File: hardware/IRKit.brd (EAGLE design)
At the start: 54 x 56 mm, 71 parts, among them CN1 ZX62-B-5PA(11), IC1 ATMEGA32U4AU, IC2 TLV70233DBVT, IC3 LM386MM-1, IC4 GS1011MXXS, SW1 EVQPUJ02K, T1 2SD1781KT146Q, T2 BSS138

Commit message: change R2,R8 value to 5.1k to reduce current
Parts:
- LED1: value 5V -> OSG50805C1C
- R2: value 910 -> 5.1k
- R8: value 1k -> 5.1k
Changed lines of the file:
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@@
 <dimension x1="22" y1="56" x2="22" y2="55" x3="21.4" y3="55.5" textsize="1.778" layer="51"/>
 <text x="47.9" y="15.1" size="0.8128" layer="21" rot="R90">+3.3V</text>
+<dimension x1="24.375" y1="5" x2="29.625" y2="5" x3="27" y3="-9" textsize="1.778" layer="51" dtype="horizontal"/>
 </plain>
 <attributes>
@@
 </autorouter>
 <elements>
-<element name="R2" library="my" package="SMD2012" value="910" x="27.85" y="50.975" smashed="yes" rot="R90">
+<element name="R2" library="my" package="SMD2012" value="5.1k" x="27.85" y="50.975" smashed="yes" rot="R90">
 <attribute name="NAME" x="27.193" y="52.901" size="0.8128" layer="25"/>
 <attribute name="VALUE" x="30.136" y="50.213" size="0.8128" layer="27" rot="R90"/>
@@
 <attribute name="VALUE" x="27.282" y="50.2115" size="0.8128" layer="27" rot="R90"/>
 </element>
-<element name="LED1" library="my" package="LED2012" value="5V" x="30.8625" y="51.925" smashed="yes">
+<element name="LED1" library="my" package="LED2012" value="OSG50805C1C" x="30.8625" y="51.925" smashed="yes">
 <attribute name="NAME" x="29.2405" y="52.941" size="0.8128" layer="25"/>
 <attribute name="VALUE" x="30.1005" y="49.639" size="0.8128" layer="27"/>
@@
 <attribute name="VALUE" x="17.086" y="14.438" size="0.8128" layer="27" rot="R90"/>
 </element>
-<element name="R8" library="my" package="SMD2012" value="1k" x="36.4" y="49.9" smashed="yes">
+<element name="R8" library="my" package="SMD2012" value="5.1k" x="36.4" y="49.9" smashed="yes">
 <attribute name="NAME" x="38.338" y="49.416" size="0.8128" layer="25"/>
 <attribute name="VALUE" x="35.638" y="47.614" size="0.8128" layer="27"/>

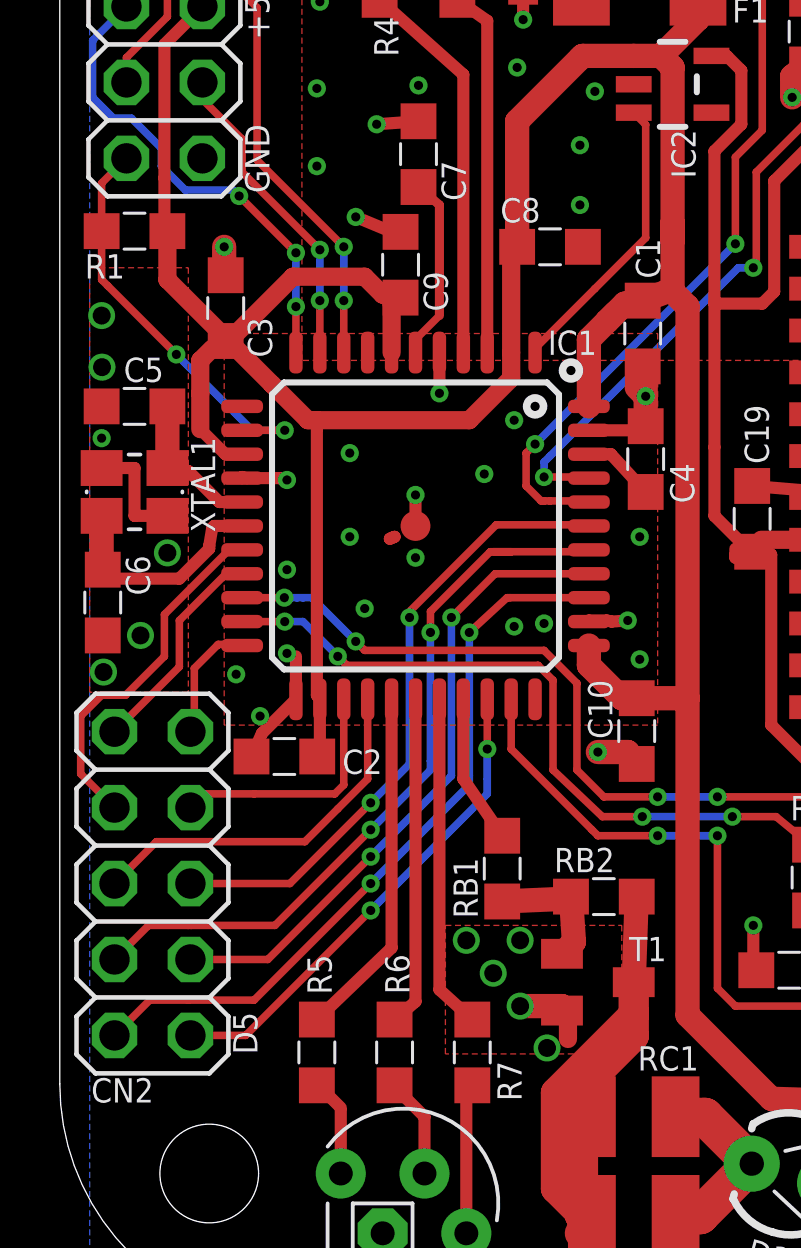
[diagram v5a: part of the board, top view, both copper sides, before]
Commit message: make lines around T1 thinner, because it took long to warm T1's emitter pad move R1 a little bit far from ICSP header, not to conflict with it
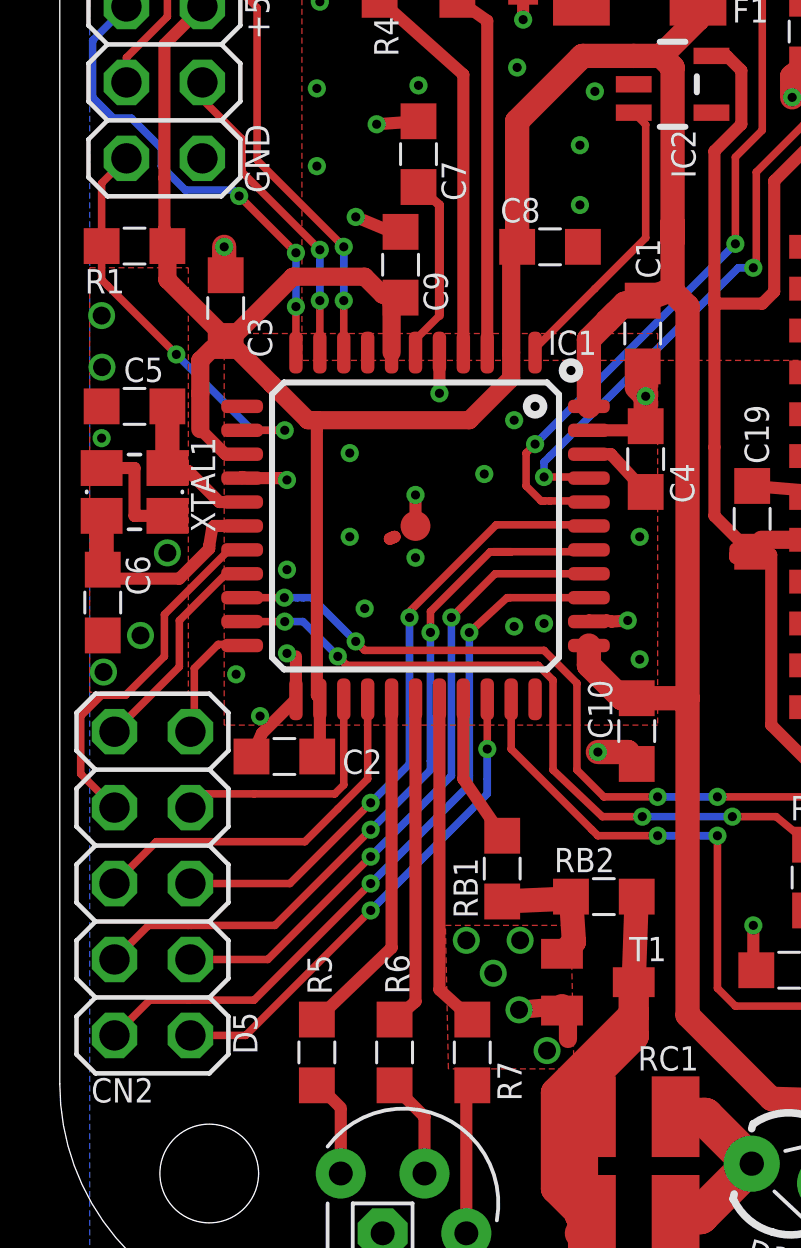
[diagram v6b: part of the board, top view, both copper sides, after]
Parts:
- moved R1 0.50 mm to (2.50, 36.0)
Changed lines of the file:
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@@
 <attribute name="VALUE" x="8.914" y="9.812" size="0.8128" layer="27" rot="R270"/>
 </element>
-<element name="R1" library="my" package="SMD2012" value="10k" x="2.5" y="36.525" smashed="yes">
-<attribute name="NAME" x="0.838" y="34.941" size="0.8128" layer="25"/>
-<attribute name="VALUE" x="0.638" y="35.739" size="0.8128" layer="27"/>
+<element name="R1" library="my" package="SMD2012" value="10k" x="2.5" y="36.025" smashed="yes">
+<attribute name="NAME" x="0.838" y="34.441" size="0.8128" layer="25"/>
+<attribute name="VALUE" x="0.638" y="35.239" size="0.8128" layer="27"/>
 </element>
 <element name="RB2" library="my" package="SMD2012" value="10k" x="18.2" y="14.2625" smashed="yes">
@@
 <wire x1="1.6" y1="34.7" x2="3.9" y2="32.4" width="0.254" layer="1"/>
 <wire x1="1.6" y1="34.7" x2="1.4" y2="34.9" width="0.254" layer="1"/>
-<wire x1="1.4" y1="34.9" x2="1.4" y2="36.525" width="0.254" layer="1"/>
-<wire x1="1.4" y1="36.525" x2="1.4" y2="38.13" width="0.254" layer="1"/>
+<wire x1="1.4" y1="34.9" x2="1.4" y2="36.025" width="0.254" layer="1"/>
+<wire x1="1.4" y1="36.025" x2="1.4" y2="38.13" width="0.254" layer="1"/>
 <wire x1="1.4" y1="38.13" x2="2.23" y2="38.96" width="0.254" layer="1"/>
 </signal>
@@
 <wire x1="17.7" y1="22" x2="17.7" y2="22.6625" width="0.8128" layer="1"/>
 <wire x1="5.55" y1="32.95" x2="3.6" y2="34.9" width="0.6096" layer="1"/>
-<wire x1="3.6" y1="34.9" x2="3.6" y2="36.525" width="0.6096" layer="1"/>
+<wire x1="3.6" y1="34.9" x2="3.6" y2="36.025" width="0.6096" layer="1"/>
 <wire x1="3.5" y1="38.3" x2="3.5" y2="36.625" width="0.4064" layer="1"/>
-<wire x1="3.5" y1="36.625" x2="3.6" y2="36.525" width="0.4064" layer="1"/>
+<wire x1="3.5" y1="36.625" x2="3.6" y2="36.025" width="0.4064" layer="1"/>
 <wire x1="19.3" y1="20.9" x2="18.8" y2="20.9" width="0.8128" layer="1"/>
 <wire x1="18.8" y1="20.9" x2="17.7" y2="22" width="0.8128" layer="1"/>
@@
 <via x="17.4" y="39.4" extent="1-16" drill="0.3048"/>
 <wire x1="19.6" y1="31" x2="19.6" y2="30" width="0.8128" layer="1"/>
-<polygon width="0.8128" layer="1">
+<polygon width="0.6096" layer="1">
 <vertex x="12.9" y="13.3"/>
-<vertex x="18.8" y="13.3"/>
-<vertex x="18.8" y="9"/>
-<vertex x="12.9" y="9"/>
+<vertex x="17.1" y="13.3"/>
+<vertex x="17.2" y="8.5"/>
+<vertex x="13" y="8.5"/>
 </polygon>
 <via x="13.6" y="53.0875" extent="1-16" drill="0.3048"/>
@@
 <wire x1="23.3" y1="11.8" x2="23.2" y2="12.1" width="0.4064" layer="1"/>
 <wire x1="23.2" y1="12.1" x2="23.2" y2="13.3" width="0.4064" layer="1"/>
-<via x="15.4" y="10.6" extent="1-16" drill="0.6"/>
+<via x="15.3625" y="10.475" extent="1-16" drill="0.6"/>
 <wire x1="31.8625" y1="51.925" x2="31.8875" y2="51.9" width="0.4064" layer="1"/>
 <wire x1="31.8875" y1="51.9" x2="33" y2="51.9" width="0.8128" layer="1"/>
@@
 <contactref element="T1" pad="E"/>
 <wire x1="16.8" y1="10.45" x2="17" y2="10.45" width="0.6096" layer="1"/>
-<wire x1="15.4" y1="10.6" x2="16.8" y2="10.6" width="0.8128" layer="1"/>
+<wire x1="15.3625" y1="10.475" x2="16.8" y2="10.6" width="0.6096" layer="1"/>
 <wire x1="16.8" y1="10.6" x2="16.8" y2="10.45" width="0.8128" layer="1"/>
 <wire x1="17" y1="10.45" x2="17" y2="9.5" width="0.6096" layer="1"/>
-<via x="16.3" y="9.2" extent="1-16" drill="0.6"/>
+<via x="16.3" y="9.1125" extent="1-16" drill="0.6"/>
 <via x="14.5" y="11.7" extent="1-16" drill="0.6"/>
 <via x="3.6" y="25.7625" extent="1-16" drill="0.6"/>

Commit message: added LED CAP
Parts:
- added LEDCAP1: LED-CAP, my:LED-CAP
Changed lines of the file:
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@@
 <attribute name="VALUE" x="0.9" y="25.55" size="1.27" layer="27"/>
 </element>
+<element name="LEDCAP1" library="my" package="LED-CAP" value="LED-CAP" x="10.8" y="-1.5"/>
 </elements>
 <signals>

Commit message: added screws updated microphone input resistor value 2k -> 2.2k change voltage dividing resistors values 2k/3.3k -> 3.3k/5.1k
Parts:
- added SCREW1, SCREW2, SCREW3, SCREW4: flat-head M3 self-tapping, my:SCREW-M3
- MIC: value kus0223 -> kus0323
- R14: value 1.3k -> 3.3k
- R15: value 2k -> 2.2k
- R16: value 2k -> 5.1k
- moved LEDCAP1 1.06 mm to (11.5, -0.70)
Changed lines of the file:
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@@
 <attribute name="VALUE" x="33.14" y="50.802" size="1.27" layer="27" ratio="10" rot="R180"/>
 </element>
-<element name="MIC" library="my" package="MIC_SMD_4MM" value="kus0223" x="42.8" y="49" smashed="yes">
+<element name="MIC" library="my" package="MIC_SMD_4MM" value="kus0323" x="42.8" y="49" smashed="yes">
 <attribute name="NAME" x="44.7" y="50.5" size="0.8128" layer="25"/>
 <attribute name="VALUE" x="44.7" y="46.8" size="0.8128" layer="27"/>
 </element>
-<element name="R15" library="my" package="SMD2012" value="2k" x="44.8" y="45.5" smashed="yes">
+<element name="R15" library="my" package="SMD2012" value="2.2k" x="44.8" y="45.5" smashed="yes">
 <attribute name="NAME" x="46.7" y="44.975" size="0.8128" layer="25"/>
 <attribute name="VALUE" x="43.8" y="43.6" size="1.016" layer="27"/>
 </element>
-<element name="R14" library="my" package="SMD2012" value="1.3k" x="44.8" y="43" smashed="yes" rot="R180">
+<element name="R14" library="my" package="SMD2012" value="3.3k" x="44.8" y="43" smashed="yes" rot="R180">
 <attribute name="NAME" x="46.7" y="42.575" size="0.8128" layer="25"/>
 <attribute name="VALUE" x="45.8" y="44.9" size="1.016" layer="27" rot="R180"/>
 </element>
-<element name="R16" library="my" package="SMD2012" value="2k" x="44.8" y="40.4" smashed="yes">
+<element name="R16" library="my" package="SMD2012" value="5.1k" x="44.8" y="40.4" smashed="yes">
 <attribute name="NAME" x="46.6875" y="39.9125" size="0.8128" layer="25"/>
 <attribute name="VALUE" x="43.8" y="38.5" size="1.016" layer="27"/>
@@
 <attribute name="VALUE" x="0.9" y="25.55" size="1.27" layer="27"/>
 </element>
-<element name="LEDCAP1" library="my" package="LED-CAP" value="LED-CAP" x="10.8" y="-1.5"/>
+<element name="LEDCAP1" library="my" package="LED-CAP" value="LED-CAP" x="11.5" y="-0.7"/>
+<element name="SCREW1" library="my" package="SCREW-M3" value="flat-head M3 self-tapping" x="-7.4" y="-11.1"/>
+<element name="SCREW2" library="my" package="SCREW-M3" value="flat-head M3 self-tapping" x="-8.4" y="-12.2"/>
+<element name="SCREW3" library="my" package="SCREW-M3" value="flat-head M3 self-tapping" x="-9.4" y="-13.3"/>
+<element name="SCREW4" library="my" package="SCREW-M3" value="flat-head M3 self-tapping" x="-10.4" y="-14.4"/>
 </elements>
 <signals>
